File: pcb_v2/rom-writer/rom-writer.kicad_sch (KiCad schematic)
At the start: 27 parts, among them J1 cartridge, Q1 IRF540N, U1 74LS574, U2 74LS193, U3 74LS193, U4 74LS125

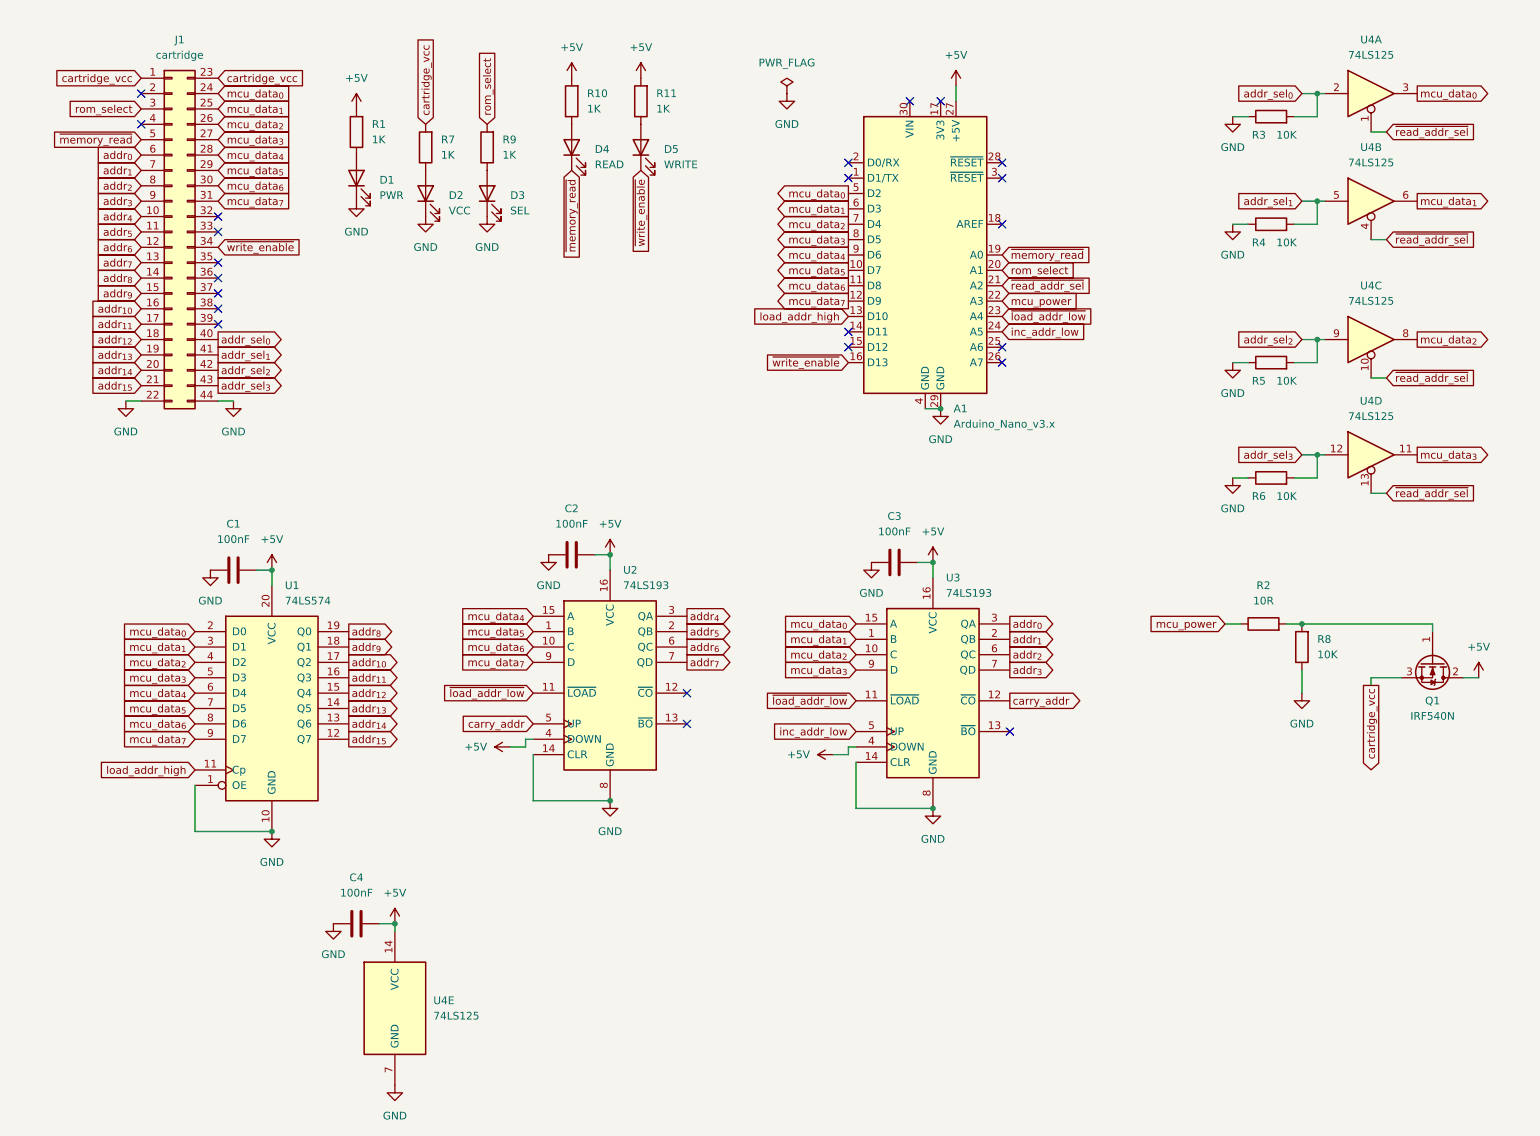
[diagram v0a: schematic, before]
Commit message: esquemático simplificado; a rom é muito lenta, endereço de escrita pode ser setado a cada ciclo
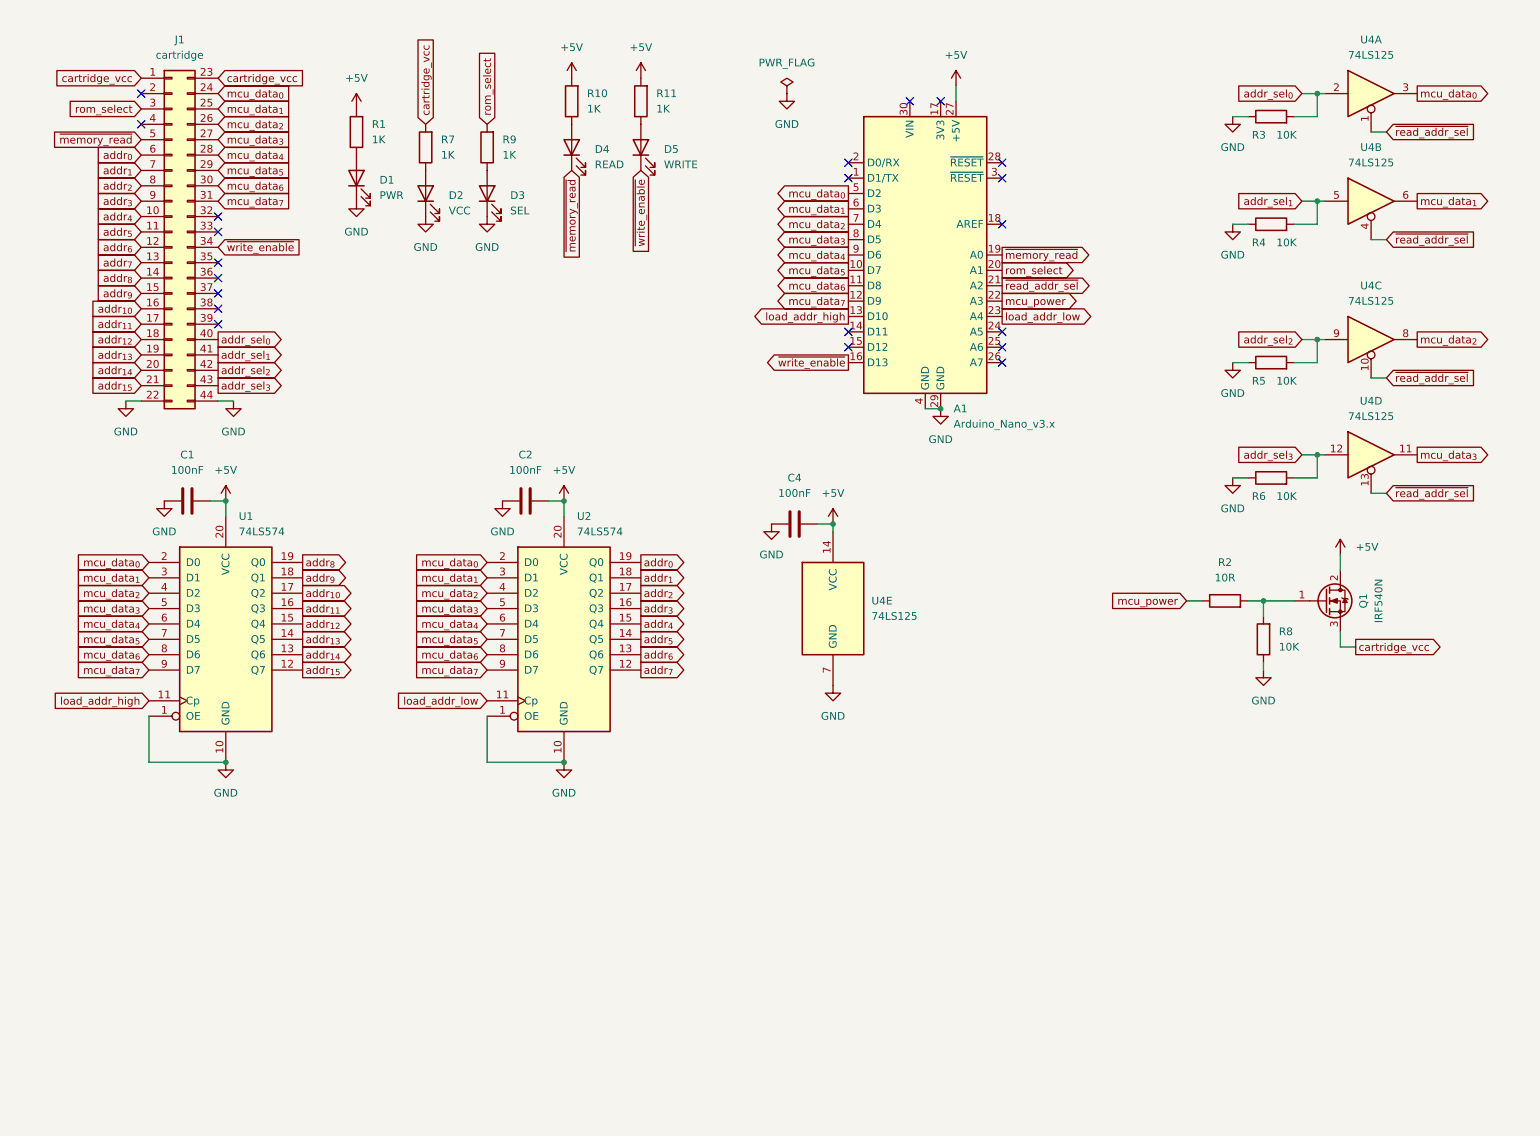
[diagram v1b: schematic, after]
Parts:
- removed C3: 100nF, Capacitor_THT:C_Disc_D5.1mm_W3.2mm_P5.00mm, symbol Device:C
- removed U2, U3: 74LS193, Package_DIP:DIP-16_W7.62mm, symbol 74xx:74LS193
- added U2: 74LS574, Package_DIP:DIP-20_W7.62mm, symbol 74xx:74LS574
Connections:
- net +5V: now also U2.20 (VCC)
- net GND: now also U2.1 (OE), U2.10 (GND)
- net addr_{0}: now also U2.19 (Q0)
- net addr_{1}: now also U2.18 (Q1)
- net addr_{2}: now also U2.17 (Q2)
- net addr_{3}: now also U2.16 (Q3)
- net addr_{4}: now also U2.15 (Q4)
- net addr_{5}: now also U2.14 (Q5)
- net addr_{6}: now also U2.13 (Q6)
- net addr_{7}: now also U2.12 (Q7)
- net mcu_data_{0}: now also U2.2 (D0)
- net mcu_data_{1}: now also U2.3 (D1)
- net mcu_data_{2}: now also U2.4 (D2)
- net mcu_data_{3}: now also U2.5 (D3)
- net mcu_data_{4}: now also U2.6 (D4)
- net mcu_data_{5}: now also U2.7 (D5)
- net mcu_data_{6}: now also U2.8 (D6)
- net mcu_data_{7}: now also U2.9 (D7)
- net inc_addr_low: no longer names the net of A1.24 (A5)
- net ~{load_addr_low} renamed load_addr_low
- net load_addr_low: now also U2.11 (Cp)
- no-connect marks 23 -> 21
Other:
- moved on the sheet: C1, C4, Q1, R2, R8, U1, U4E
